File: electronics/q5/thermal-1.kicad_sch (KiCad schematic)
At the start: 6 parts, among them Q3 Charge enable, Q4 Charge enable hot gate

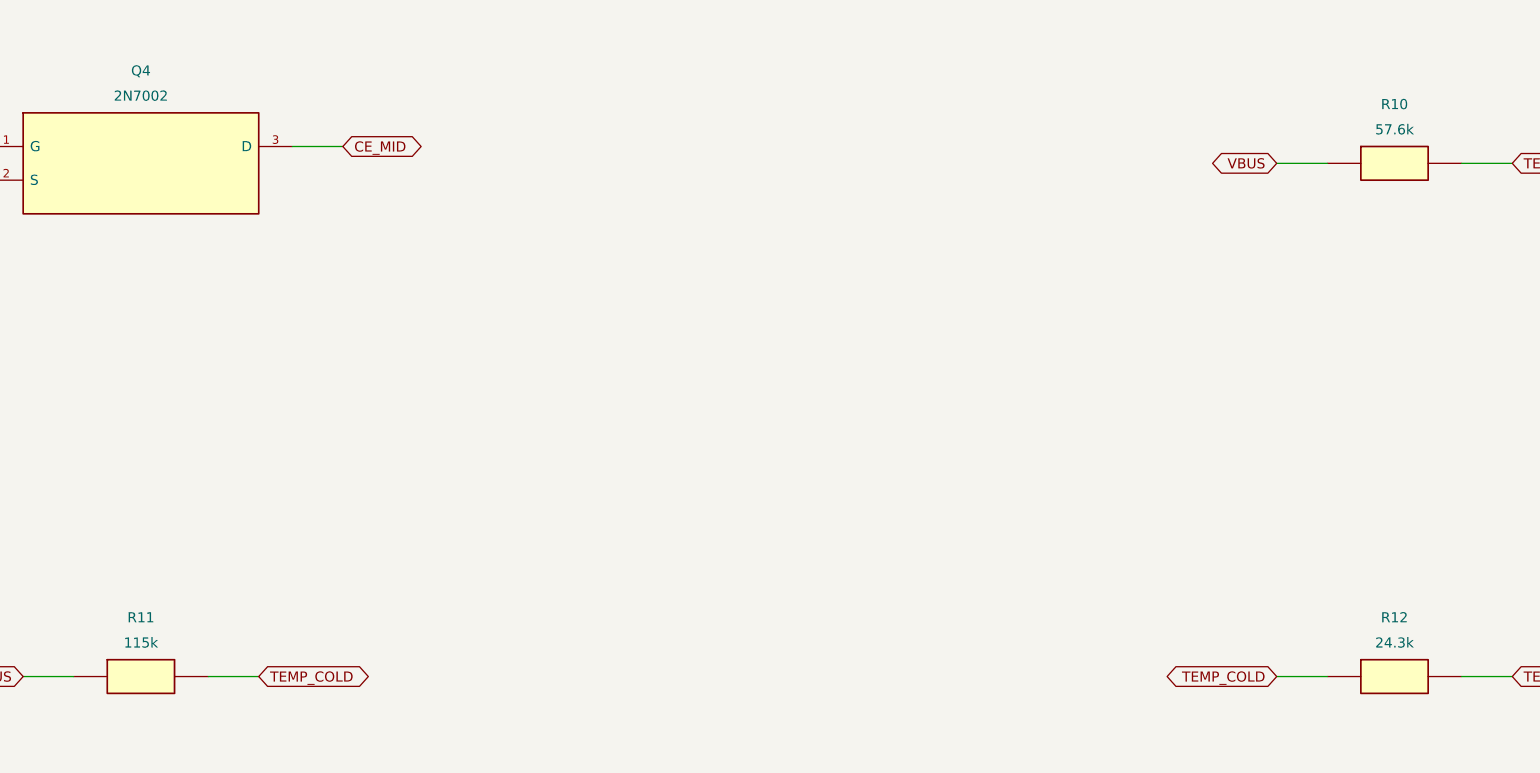
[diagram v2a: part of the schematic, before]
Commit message: Move nine part types to JLC Basic; 16 Extended types remain, each justified
R4 18k (16.7 mA charge), temperature window 56k/82k/18k/12k (7.26-35.83 C),
R32 75 ohm, Q1/Q2 AO3400A, 2.2 uF and 10 uF 50 V 0805 capacitors. Fresh
ERC/DRC/parity on unchanged routing, stock 42/42, exports, JLC footprint
fit and pin names, power/latch checks re-run. About $28 less per order.

Co-Authored-By: Claude Opus 5.5 <noreply@anthropic.com>
Claude-Session: https://claude.ai/code/session_01UrkzLMrBi6iLPSL5SbMCA7
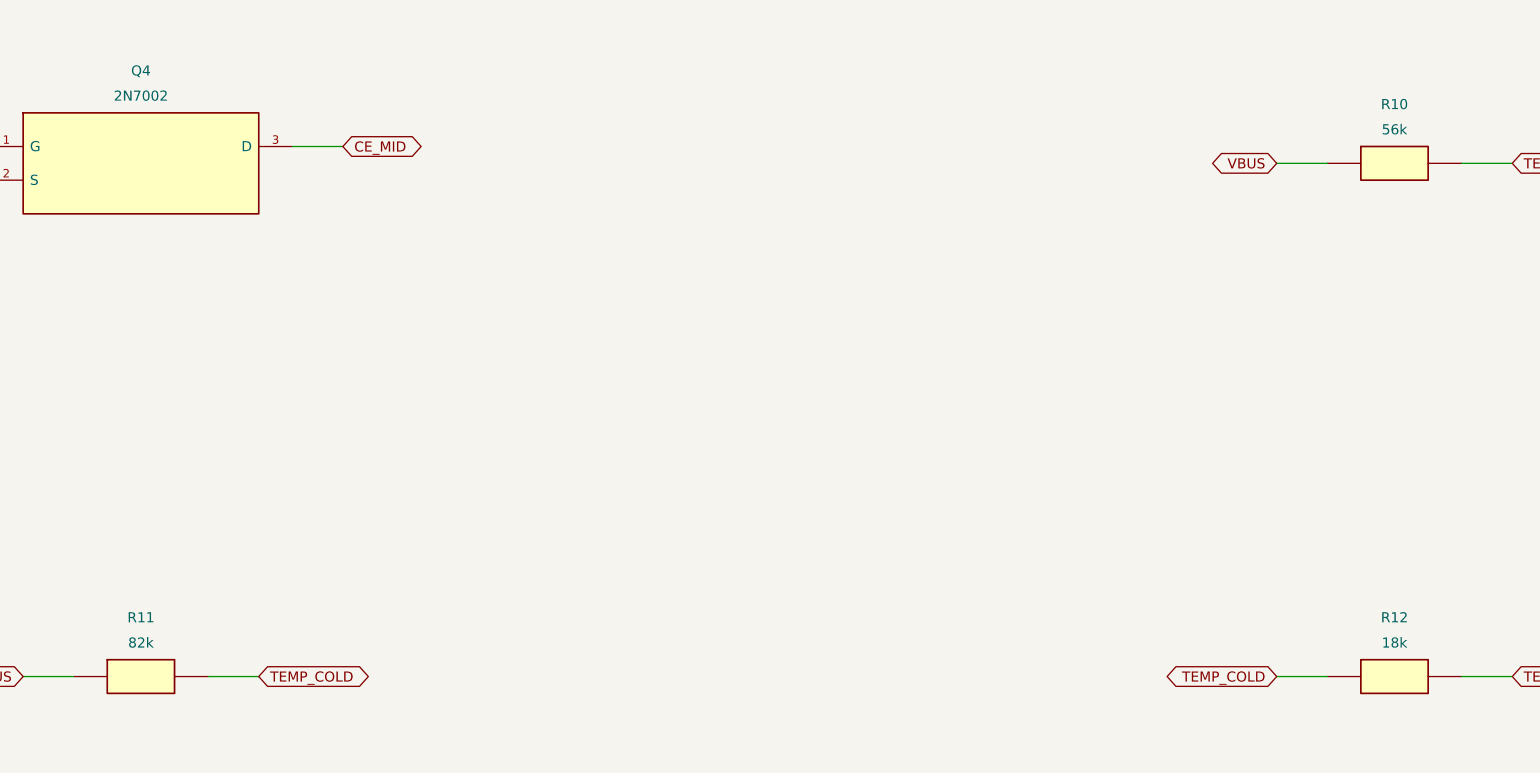
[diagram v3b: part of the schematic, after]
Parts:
- R10: value 57.6k -> 56k; MPN RC0603FR-0757K6L -> 0603WAF5602T5E
- R11: value 115k -> 82k; MPN 0603WAF1153T5E -> 0603WAF8202T5E
- R12: value 24.3k -> 18k; MPN RC0603FR-0724K3L -> 0603WAF1802T5E
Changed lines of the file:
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@@
 (symbol (lib_id "CountFidgetQ5:R10") (at 294.64 161.29 0) (unit 1) (exclude_from_sim no)
       (in_bom yes) (on_board yes) (dnp no)
- (property "Reference" "R10" (at 294.64 152.4 0) (effects (font (size 1.524 1.524)))) (property "Value" "57.6k" (at 294.64 156.21 0) (effects (font (size 1.524 1.524))))
-      (property "Footprint" "CountFidgetQ5:Resistor_SMD_R_0603_1608Metric" (at 294.64 161.29 0) (effects (font (size 1.27 1.27)) (hide yes))) (property "MPN" "RC0603FR-0757K6L" (at 294.64 156.21 0) (effects (font (size 1.524 1.524)) (hide yes)))
+ (property "Reference" "R10" (at 294.64 152.4 0) (effects (font (size 1.524 1.524)))) (property "Value" "56k" (at 294.64 156.21 0) (effects (font (size 1.524 1.524))))
+      (property "Footprint" "CountFidgetQ5:Resistor_SMD_R_0603_1608Metric" (at 294.64 161.29 0) (effects (font (size 1.27 1.27)) (hide yes))) (property "MPN" "0603WAF5602T5E" (at 294.64 156.21 0) (effects (font (size 1.524 1.524)) (hide yes)))
       (property "Description" "1%, 0603, 0.1 W" (at 294.64 161.29 0) (effects (font (size 1.27 1.27)) (hide yes)))
       (pin "1")(pin "2")
@@
 (symbol (lib_id "CountFidgetQ5:R11") (at 105.41 238.76 0) (unit 1) (exclude_from_sim no)
       (in_bom yes) (on_board yes) (dnp no)
- (property "Reference" "R11" (at 105.41 229.87 0) (effects (font (size 1.524 1.524)))) (property "Value" "115k" (at 105.41 233.68 0) (effects (font (size 1.524 1.524))))
-      (property "Footprint" "CountFidgetQ5:Resistor_SMD_R_0603_1608Metric" (at 105.41 238.76 0) (effects (font (size 1.27 1.27)) (hide yes))) (property "MPN" "0603WAF1153T5E" (at 105.41 233.68 0) (effects (font (size 1.524 1.524)) (hide yes)))
+ (property "Reference" "R11" (at 105.41 229.87 0) (effects (font (size 1.524 1.524)))) (property "Value" "82k" (at 105.41 233.68 0) (effects (font (size 1.524 1.524))))
+      (property "Footprint" "CountFidgetQ5:Resistor_SMD_R_0603_1608Metric" (at 105.41 238.76 0) (effects (font (size 1.27 1.27)) (hide yes))) (property "MPN" "0603WAF8202T5E" (at 105.41 233.68 0) (effects (font (size 1.524 1.524)) (hide yes)))
       (property "Description" "1%, 0603, 0.1 W" (at 105.41 238.76 0) (effects (font (size 1.27 1.27)) (hide yes)))
       (pin "1")(pin "2")
@@
 (symbol (lib_id "CountFidgetQ5:R12") (at 294.64 238.76 0) (unit 1) (exclude_from_sim no)
       (in_bom yes) (on_board yes) (dnp no)
- (property "Reference" "R12" (at 294.64 229.87 0) (effects (font (size 1.524 1.524)))) (property "Value" "24.3k" (at 294.64 233.68 0) (effects (font (size 1.524 1.524))))
-      (property "Footprint" "CountFidgetQ5:Resistor_SMD_R_0603_1608Metric" (at 294.64 238.76 0) (effects (font (size 1.27 1.27)) (hide yes))) (property "MPN" "RC0603FR-0724K3L" (at 294.64 233.68 0) (effects (font (size 1.524 1.524)) (hide yes)))
+ (property "Reference" "R12" (at 294.64 229.87 0) (effects (font (size 1.524 1.524)))) (property "Value" "18k" (at 294.64 233.68 0) (effects (font (size 1.524 1.524))))
+      (property "Footprint" "CountFidgetQ5:Resistor_SMD_R_0603_1608Metric" (at 294.64 238.76 0) (effects (font (size 1.27 1.27)) (hide yes))) (property "MPN" "0603WAF1802T5E" (at 294.64 233.68 0) (effects (font (size 1.524 1.524)) (hide yes)))
       (property "Description" "1%, 0603, 0.1 W" (at 294.64 238.76 0) (effects (font (size 1.27 1.27)) (hide yes)))
       (pin "1")(pin "2")
